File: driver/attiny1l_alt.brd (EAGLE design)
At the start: 26.9 x 17.3 mm, 6 parts, among them IC1 ATTiny85, IC3 74AHC1G00DCK, IC4 LB1973M, J1 AVR_SPI_PRG_6NS

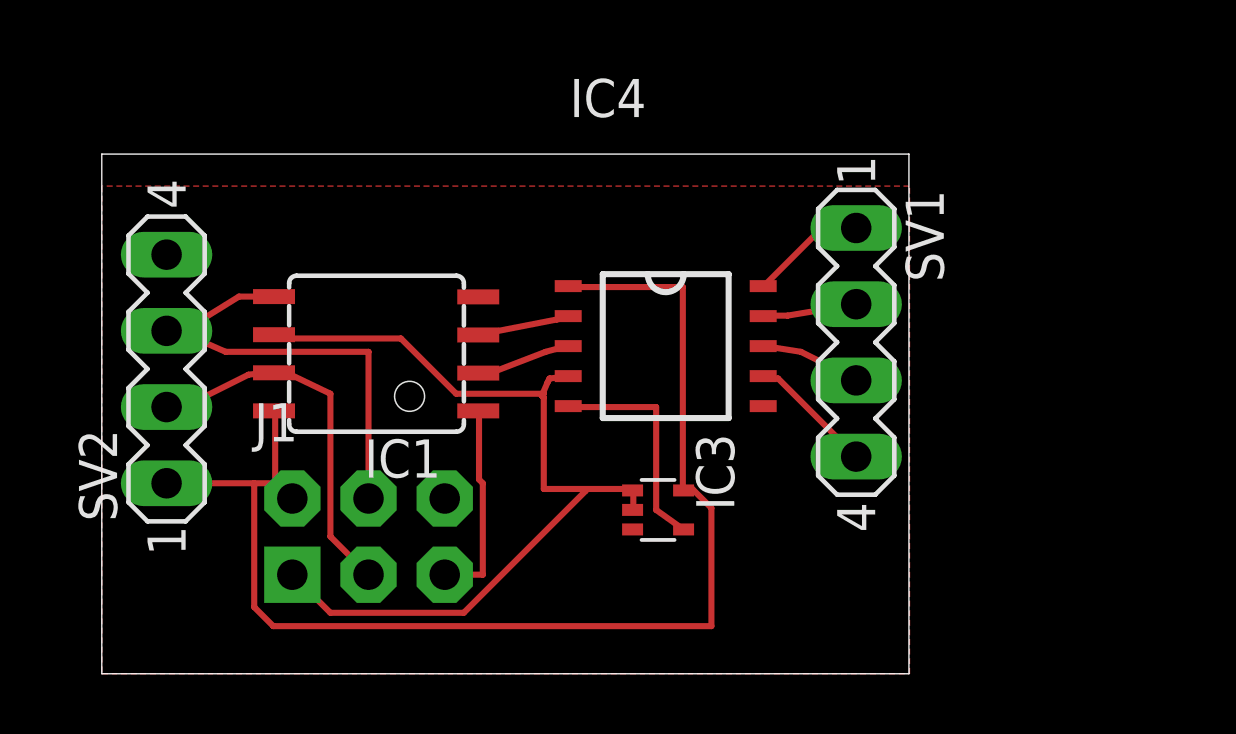
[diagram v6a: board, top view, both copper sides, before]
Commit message: the footpring was actually a bit too wide, made it 20mils narrower
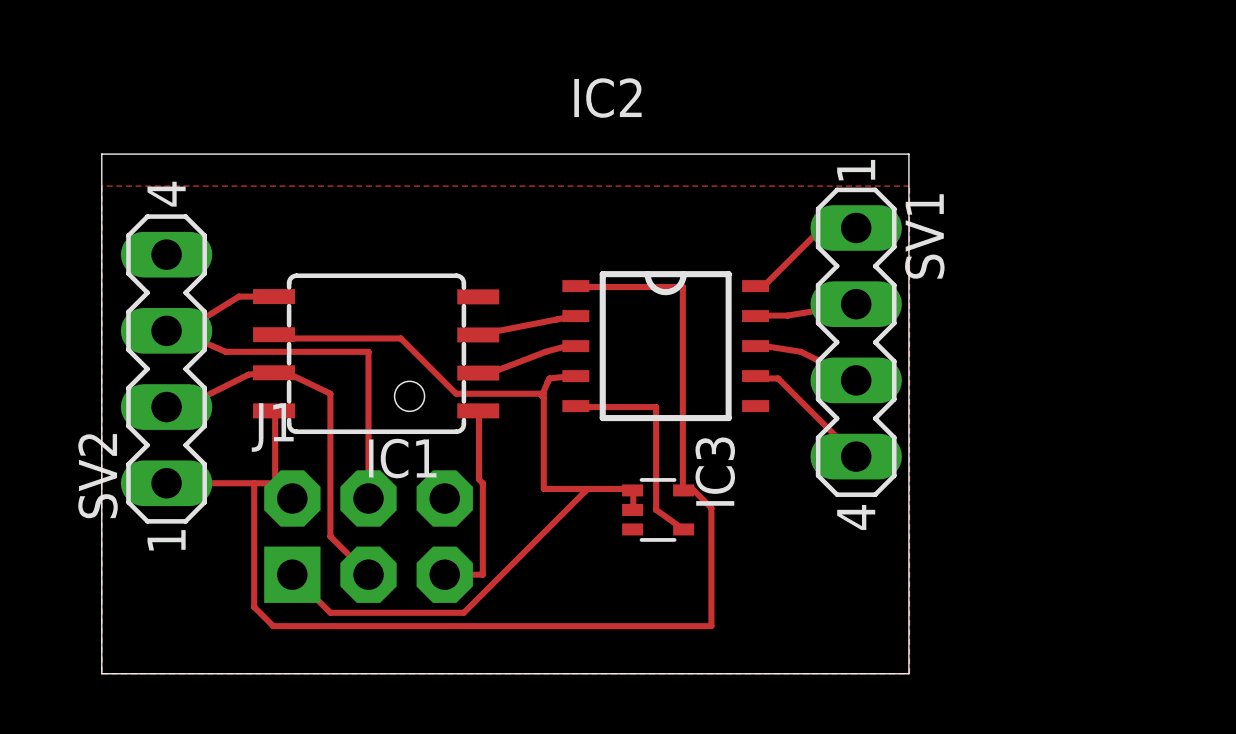
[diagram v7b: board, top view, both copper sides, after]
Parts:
- renumbered IC4 to IC2
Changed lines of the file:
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@@
 <attribute name="OC_FARNELL" value="unknown" x="47.879" y="44.45" size="1.778" layer="27" rot="R90" display="off"/>
 </element>
-<element name="IC4" library="LB1973M" package="SSOP10" value="LB1973M" x="18.796" y="10.922"/>
+<element name="IC2" library="LB1973M" package="SSOP10" value="LB1973M" x="18.796" y="10.922"/>
 </elements>
 <signals>
 <signal name="IN2">
 <contactref element="IC3" pad="4"/>
-<contactref element="IC4" pad="5"/>
 <wire x1="18.4785" y1="5.461" x2="19.3675" y2="4.826" width="0.2032" layer="1"/>
 <wire x1="18.4785" y1="8.89" x2="18.4785" y2="5.461" width="0.2032" layer="1"/>
-<wire x1="15.5575" y1="8.89" x2="18.4785" y2="8.89" width="0.2032" layer="1"/>
+<wire x1="15.5575" y1="8.89" x2="15.8115" y2="8.89" width="0.2032" layer="1"/>
+<wire x1="15.8115" y1="8.89" x2="18.4785" y2="8.89" width="0.2032" layer="1"/>
 <wire x1="19.3675" y1="4.826" x2="19.392" y2="4.811" width="0.2032" layer="1"/>
-<wire x1="15.5575" y1="8.89" x2="15.546" y2="8.922" width="0.2032" layer="1"/>
+<contactref element="IC2" pad="5"/>
+<wire x1="15.8115" y1="8.9535" x2="15.8" y2="8.922" width="0.2032" layer="1"/>
+<wire x1="15.8115" y1="8.9535" x2="15.8115" y2="8.89" width="0.2032" layer="1"/>
 </signal>
 <signal name="IN4">
-<contactref element="IC4" pad="2"/>
 <contactref element="IC1" pad="3"/>
 <wire x1="15.1765" y1="11.811" x2="15.494" y2="11.8745" width="0.2032" layer="1"/>
 <wire x1="12.573" y1="11.303" x2="15.1765" y2="11.811" width="0.2032" layer="1"/>
-<wire x1="15.494" y1="11.8745" x2="15.546" y2="11.922" width="0.2032" layer="1"/>
 <wire x1="12.573" y1="11.303" x2="12.548" y2="11.293" width="0.2032" layer="1"/>
+<contactref element="IC2" pad="2"/>
+<wire x1="15.5575" y1="11.938" x2="15.748" y2="11.938" width="0.2032" layer="1"/>
+<wire x1="15.748" y1="11.938" x2="15.8" y2="11.922" width="0.2032" layer="1"/>
+<wire x1="15.5575" y1="11.938" x2="15.494" y2="11.8745" width="0.2032" layer="1"/>
 </signal>
 <signal name="IN1/MISO">
@@
 <contactref element="IC1" pad="6"/>
 <contactref element="J1" pad="1"/>
-<contactref element="IC4" pad="4"/>
 <wire x1="17.7165" y1="6.096" x2="17.7165" y2="5.461" width="0.2032" layer="1"/>
 <wire x1="17.7165" y1="5.461" x2="17.692" y2="5.461" width="0.2032" layer="1"/>
@@
 <wire x1="17.653" y1="6.1595" x2="16.129" y2="6.1595" width="0.2032" layer="1"/>
 <wire x1="16.129" y1="6.1595" x2="14.732" y2="6.1595" width="0.2032" layer="1"/>
-<wire x1="15.494" y1="9.906" x2="15.546" y2="9.922" width="0.2032" layer="1"/>
 <wire x1="17.653" y1="6.1595" x2="17.692" y2="6.111" width="0.2032" layer="1"/>
 <wire x1="5.9055" y1="11.176" x2="5.7785" y2="11.303" width="0.2032" layer="1"/>
@@
 <wire x1="16.129" y1="6.096" x2="12.065" y2="2.032" width="0.2032" layer="1"/>
 <wire x1="16.129" y1="6.096" x2="16.129" y2="6.1595" width="0.2032" layer="1"/>
+<contactref element="IC2" pad="4"/>
+<wire x1="15.494" y1="9.906" x2="15.748" y2="9.906" width="0.2032" layer="1"/>
+<wire x1="15.748" y1="9.906" x2="15.8" y2="9.922" width="0.2032" layer="1"/>
 </signal>
 <signal name="IN3">
-<contactref element="IC4" pad="3"/>
 <contactref element="IC1" pad="2"/>
 <wire x1="14.7955" y1="10.7315" x2="15.494" y2="10.922" width="0.2032" layer="1"/>
 <wire x1="13.1445" y1="10.0965" x2="14.7955" y2="10.7315" width="0.2032" layer="1"/>
 <wire x1="12.573" y1="10.033" x2="13.1445" y2="10.0965" width="0.2032" layer="1"/>
-<wire x1="15.494" y1="10.922" x2="15.546" y2="10.922" width="0.2032" layer="1"/>
 <wire x1="12.573" y1="10.033" x2="12.548" y2="10.023" width="0.2032" layer="1"/>
+<contactref element="IC2" pad="3"/>
+<wire x1="15.494" y1="10.922" x2="15.8" y2="10.922" width="0.2032" layer="1"/>
 </signal>
 <signal name="GND">
@@
 <contactref element="J1" pad="6"/>
 <contactref element="SV2" pad="4"/>
-<contactref element="IC4" pad="6"/>
-<contactref element="IC4" pad="6"/>
 <polygon width="0.2032" layer="1" isolate="0.4064">
 <vertex x="0" y="16.256"/>
@@
 <vertex x="26.924" y="16.256"/>
 </polygon>
-<wire x1="22.046" y1="8.922" x2="17.692" y2="4.811" width="0" layer="19" extent="1-1"/>
+<contactref element="IC2" pad="6"/>
+<contactref element="IC2" pad="6"/>
+<wire x1="21.792" y1="8.922" x2="17.692" y2="4.811" width="0" layer="19" extent="1-1"/>
 <wire x1="11.43" y1="5.842" x2="17.692" y2="4.811" width="0" layer="19" extent="1-1"/>
 </signal>
@@
 <contactref element="J1" pad="2"/>
 <contactref element="SV2" pad="1"/>
-<contactref element="IC4" pad="1"/>
 <wire x1="19.3675" y1="12.8905" x2="19.3675" y2="6.1595" width="0.2032" layer="1"/>
-<wire x1="15.5575" y1="12.8905" x2="19.3675" y2="12.8905" width="0.2032" layer="1"/>
+<wire x1="15.5575" y1="12.8905" x2="15.8115" y2="12.8905" width="0.2032" layer="1"/>
+<wire x1="15.8115" y1="12.8905" x2="19.3675" y2="12.8905" width="0.2032" layer="1"/>
 <wire x1="19.3675" y1="6.1595" x2="19.392" y2="6.111" width="0.2032" layer="1"/>
-<wire x1="15.5575" y1="12.8905" x2="15.546" y2="12.922" width="0.2032" layer="1"/>
 <wire x1="5.7785" y1="5.842" x2="5.7785" y2="8.763" width="0.2032" layer="1"/>
 <wire x1="6.35" y1="5.842" x2="5.7785" y2="5.842" width="0.2032" layer="1"/>
@@
 <wire x1="5.08" y1="6.35" x2="5.08" y2="2.2225" width="0.2032" layer="1"/>
 <wire x1="19.685" y1="6.1595" x2="19.392" y2="6.111" width="0.2032" layer="1"/>
+<contactref element="IC2" pad="1"/>
+<wire x1="15.8115" y1="12.954" x2="15.8" y2="12.922" width="0.2032" layer="1"/>
+<wire x1="15.8115" y1="12.954" x2="15.8115" y2="12.8905" width="0.2032" layer="1"/>
 </signal>
 <signal name="SDA/MOSI">
@@
 <signal name="OUT4">
 <contactref element="SV1" pad="1"/>
-<contactref element="IC4" pad="10"/>
 <wire x1="24.003" y1="14.859" x2="22.098" y2="12.954" width="0.2032" layer="1"/>
 <wire x1="25.146" y1="14.859" x2="24.003" y2="14.859" width="0.2032" layer="1"/>
-<wire x1="22.098" y1="12.954" x2="22.046" y2="12.922" width="0.2032" layer="1"/>
+<contactref element="IC2" pad="10"/>
+<wire x1="22.098" y1="12.954" x2="21.844" y2="12.954" width="0.2032" layer="1"/>
+<wire x1="21.844" y1="12.954" x2="21.792" y2="12.922" width="0.2032" layer="1"/>
 </signal>
 <signal name="OUT3">
 <contactref element="SV1" pad="2"/>
-<contactref element="IC4" pad="9"/>
-<wire x1="22.86" y1="11.938" x2="22.098" y2="11.938" width="0.2032" layer="1"/>
+<wire x1="22.86" y1="11.938" x2="21.844" y2="11.938" width="0.2032" layer="1"/>
 <wire x1="25.146" y1="12.319" x2="22.86" y2="11.938" width="0.2032" layer="1"/>
-<wire x1="22.098" y1="11.938" x2="22.046" y2="11.922" width="0.2032" layer="1"/>
+<contactref element="IC2" pad="9"/>
+<wire x1="21.844" y1="11.938" x2="21.792" y2="11.922" width="0.2032" layer="1"/>
 </signal>
 <signal name="OUT1">
 <contactref element="SV1" pad="3"/>
-<contactref element="IC4" pad="8"/>
 <wire x1="23.3045" y1="10.7315" x2="22.098" y2="10.922" width="0.2032" layer="1"/>
 <wire x1="24.3205" y1="10.2235" x2="23.3045" y2="10.7315" width="0.2032" layer="1"/>
 <wire x1="25.146" y1="9.779" x2="24.3205" y2="10.2235" width="0.2032" layer="1"/>
-<wire x1="22.098" y1="10.922" x2="22.046" y2="10.922" width="0.2032" layer="1"/>
+<contactref element="IC2" pad="8"/>
+<wire x1="22.098" y1="10.922" x2="21.792" y2="10.922" width="0.2032" layer="1"/>
 </signal>
 <signal name="OUT2">
 <contactref element="SV1" pad="4"/>
-<contactref element="IC4" pad="7"/>
 <wire x1="22.1615" y1="9.8425" x2="22.098" y2="9.906" width="0.2032" layer="1"/>
 <wire x1="22.5425" y1="9.8425" x2="22.1615" y2="9.8425" width="0.2032" layer="1"/>
 <wire x1="25.146" y1="7.239" x2="22.5425" y2="9.8425" width="0.2032" layer="1"/>
-<wire x1="22.098" y1="9.906" x2="22.046" y2="9.922" width="0.2032" layer="1"/>
+<contactref element="IC2" pad="7"/>
+<wire x1="22.098" y1="9.906" x2="21.844" y2="9.906" width="0.2032" layer="1"/>
+<wire x1="21.844" y1="9.906" x2="21.792" y2="9.922" width="0.2032" layer="1"/>
 </signal>
 </signals>

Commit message: added bypass caps, hopefully it helps with the weird clock/reset issues we are having
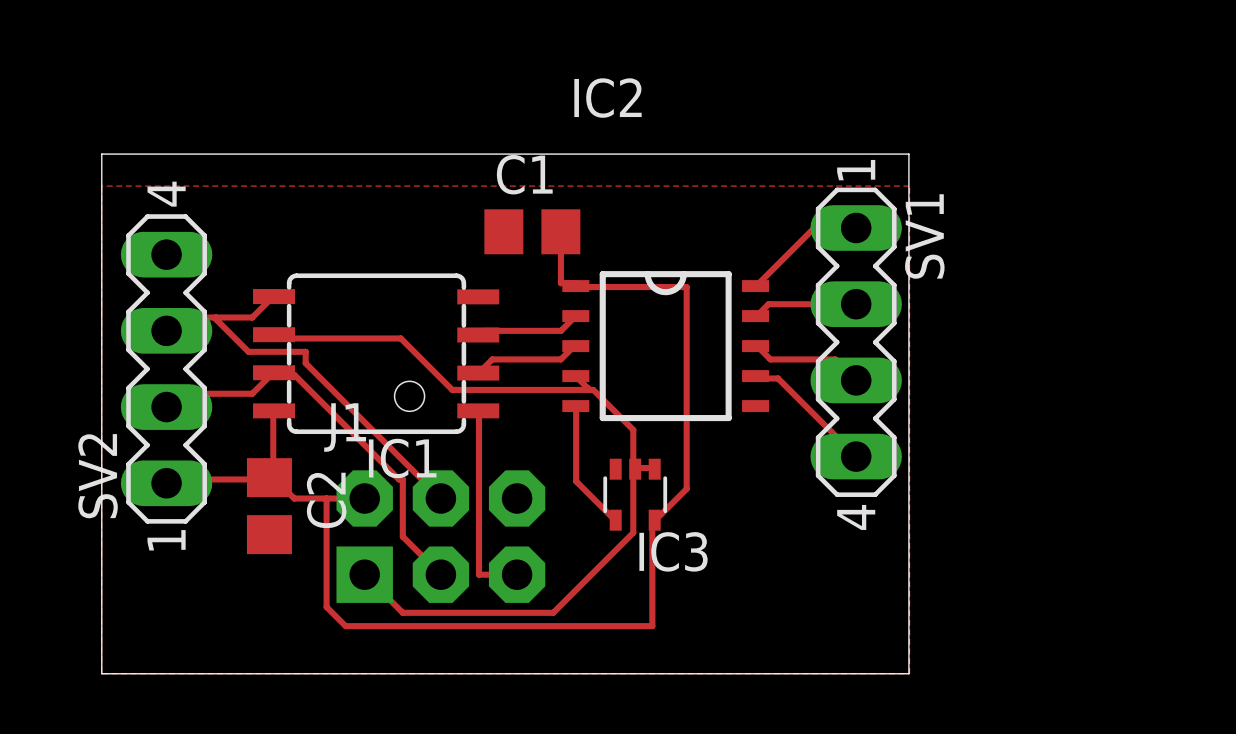
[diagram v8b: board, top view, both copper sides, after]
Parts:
- added C1, C2: (no value), rcl:C0805
- moved J1 2.41 mm to (11.3, 4.57)
- moved IC3 0.92 mm to (17.8, 5.97), turned to 180 degrees
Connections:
- net +5V: now also C1.2, C2.1
- net GND: now also C1.1, C2.2
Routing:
- net IN2: track 7.57 -> 4.36 mm
- net IN1/MISO: track 30.3 -> 28.7 mm
- net +5V: track 43.4 -> 41.9 mm
- net SDA/MOSI: track 15.4 -> 14.3 mm
- net SCL/SCK: track 12.8 -> 13.5 mm
